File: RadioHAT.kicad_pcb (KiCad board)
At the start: 2 copper layers, 65 x 56.5 mm, 37 parts, among them J1 RPi_GPIO, J3 Conn_02x06_Odd_Even, J4 Conn_02x07_Odd_Even, U1 INA219AxD, U2 LP3855-ADJ

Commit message: [PCB] Add jumper texts
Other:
- board text added: "INA_BYPASS"
- board text added: "PWR_LDO"
- board text added: "PWR_RPI"
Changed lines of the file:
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@@
 			(at 0 1.8288 0)
 			(layer "F.SilkS")
+			(hide yes)
 			(effects
 				(font
@@
 			(at 0 -1.8 90)
 			(layer "F.SilkS")
+			(hide yes)
 			(effects
 				(font
@@
 			(layer "F.CrtYd")
 		)
-		(fp_text user "3"
-			(at 2.6 0 90)
-			(layer "F.SilkS")
-			(effects
-				(font
-					(size 1 1)
-					(thickness 0.15)
-				)
-			)
-		)
-		(fp_text user "1"
-			(at -2.6 0 90)
-			(layer "F.SilkS")
-			(effects
-				(font
-					(size 1 1)
-					(thickness 0.15)
-				)
-			)
-		)
 		(pad "1" smd rect
 			(at -1.3 0 270)
@@
 			(at 0 -1.8 90)
 			(layer "F.SilkS")
+			(hide yes)
 			(effects
 				(font
@@
 			(layer "F.CrtYd")
 		)
-		(fp_text user "3"
-			(at 2.6 0 90)
-			(layer "F.SilkS")
-			(effects
-				(font
-					(size 1 1)
-					(thickness 0.15)
-				)
-			)
-		)
-		(fp_text user "1"
-			(at -2.6 0 90)
-			(layer "F.SilkS")
-			(effects
-				(font
-					(size 1 1)
-					(thickness 0.15)
-				)
-			)
-		)
 		(pad "1" smd rect
 			(at -1.3 0 270)
@@
 			(at 0 -1.8 90)
 			(layer "F.SilkS")
+			(hide yes)
 			(effects
 				(font
@@
 			(layer "F.CrtYd")
 		)
-		(fp_text user "1"
-			(at -2.6 0 90)
-			(layer "F.SilkS")
-			(effects
-				(font
-					(size 1 1)
-					(thickness 0.15)
-				)
-			)
-		)
-		(fp_text user "3"
-			(at 2.6 0 90)
-			(layer "F.SilkS")
-			(effects
-				(font
-					(size 1 1)
-					(thickness 0.15)
-				)
-			)
-		)
 		(pad "1" smd rect
 			(at -1.3 0 270)
@@
 		)
 	)
+	(gr_text "PWR_LDO"
+		(at 149.7584 90.6272 0)
+		(layer "F.SilkS")
+		(effects
+			(font
+				(size 0.6 0.6)
+				(thickness 0.1)
+			)
+			(justify left)
+		)
+	)
+	(gr_text "INA_BYPASS"
+		(at 157.6324 90.0684 0)
+		(layer "F.SilkS")
+		(effects
+			(font
+				(size 0.6 0.6)
+				(thickness 0.1)
+			)
+			(justify bottom)
+		)
+	)
+	(gr_text "PWR_RPI"
+		(at 149.8092 92.3036 0)
+		(layer "F.SilkS")
+		(effects
+			(font
+				(size 0.6 0.6)
+				(thickness 0.1)
+			)
+			(justify left)
+		)
+	)

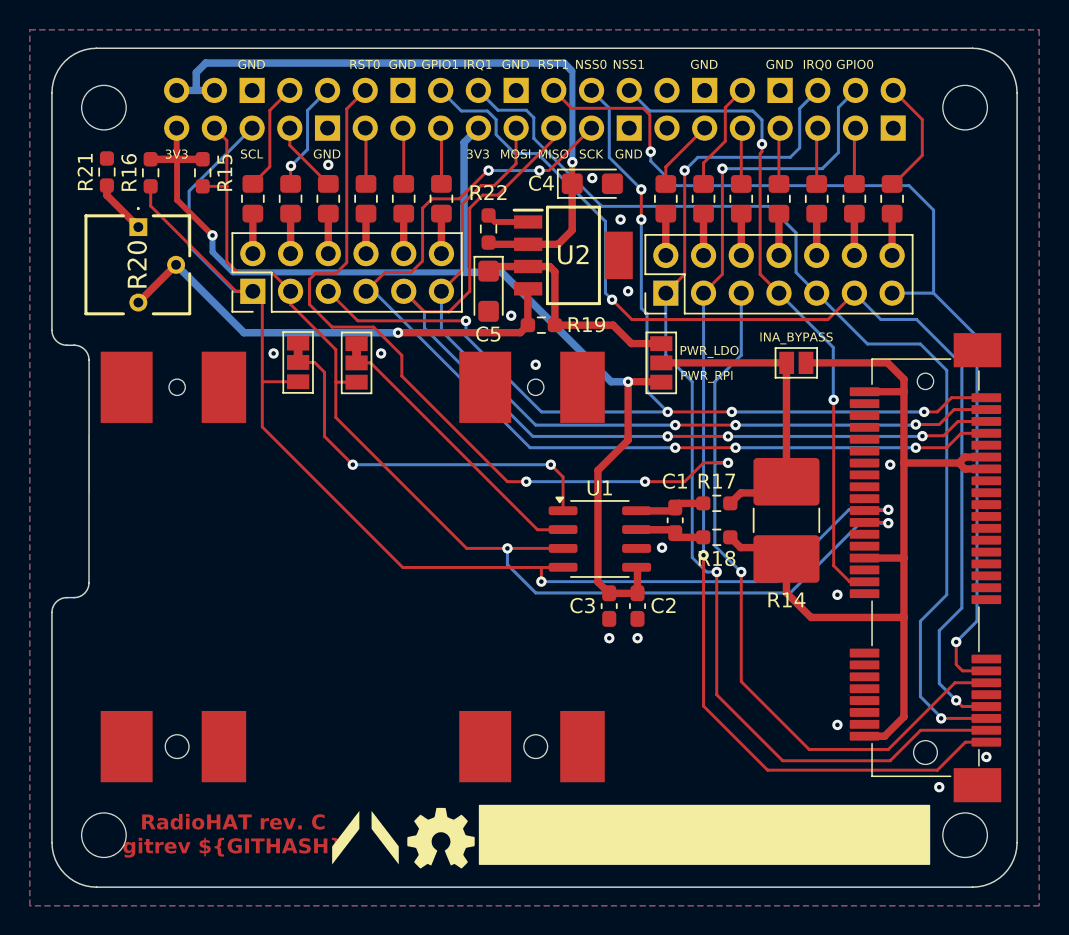
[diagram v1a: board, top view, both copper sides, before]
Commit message: Implemented @RemyChatel recommendations
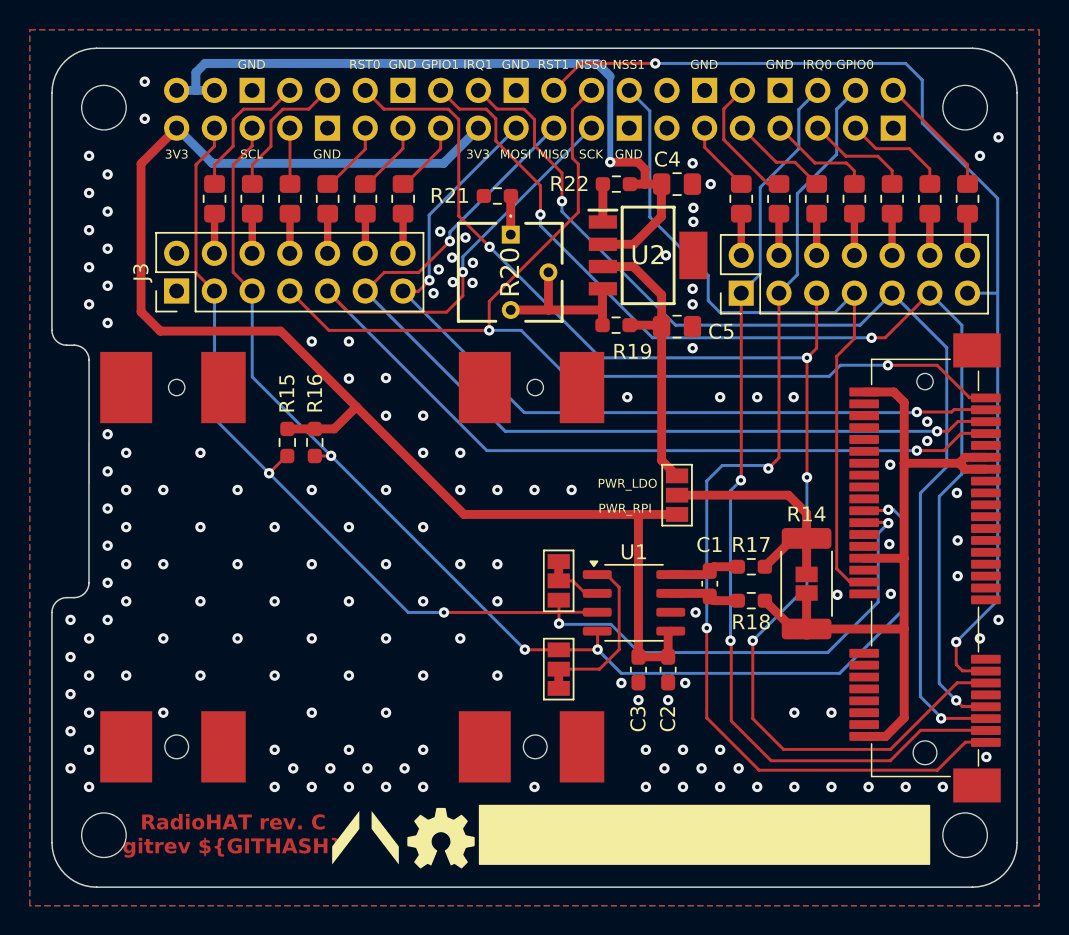
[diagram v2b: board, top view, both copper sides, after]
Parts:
- removed JP4: SolderJumper_2_Open, Jumper:SolderJumper-2_P1.3mm_Open_Pad1.0x1.5mm
- C4, C5: value 10u -> 100n; footprint Capacitor_Tantalum_SMD:CP_EIA-3216-18_Kemet-A -> Capacitor_SMD:C_0805_2012Metric_Pad1.18x1.45mm_HandSolder
- J3: value Conn_02x06_Odd_Even -> Conn_02x07_Odd_Even; footprint Connector_PinHeader_2.54mm:PinHeader_2x06_P2.54mm_Vertical -> Connector_PinHeader_2.54mm:PinHeader_2x07_P2.54mm_Vertical
- R14: footprint Resistor_SMD:R_2816_7142Metric_Pad3.20x4.45mm_HandSolder -> RadioHAT:R_2512_6332Metric_Pad1.40x3.35mm_HandSolder_Bypass
- R19: value 100R -> 10k
- R20: value 18R -> 2k; footprint RadioHAT:3362P1200LF -> RadioHAT:Potentiometer_Bourns_3362P1200LF
- R21: value 51R -> 6.8k
- moved JP2 27.1 mm to (141.6, 112.1), turned to 90 degrees
- moved R21 26.3 mm to (137.5, 80.2), turned to 180 degrees
- moved R20 25.1 mm to (138.4, 82.8)
- moved R16 21.3 mm to (125.2, 96.8)
- moved JP1 20.0 mm to (141.6, 106.1)
- moved R15 19.0 mm to (123.3, 96.8)
- moved C5 12.9 mm to (149.6, 89.0), turned to 0 degrees
- moved R22 9.13 mm to (145.5, 79.4), turned to 180 degrees
- moved JP5 8.97 mm to (149.6, 100.3)
- moved C4 5.71 mm to (149.6, 79.4)
- moved J3 5.13 mm to (115.9, 86.6)
- moved J4 5.08 mm to (153.9, 86.7)
- moved R10 5.08 mm to (161.5, 80.4)
- moved R11 5.08 mm to (164.1, 80.4)
- moved R7 5.08 mm to (153.9, 80.4)
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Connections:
- J1 pad 10: SDA_SENSE -> SCL_SENSE
- J1 pad 8: SCL_SENSE -> SDA_SENSE
- J3 pad 1: SCL -> GND
- J3 pad 11: MOSI -> MISO
- J3 pad 2: Net-(J3-Pin_2) -> GND
- J3 pad 5: NSS0 -> SCL
- J3 pad 7: SCK -> NSS0
- J3 pad 9: MISO -> SCK
- R1 pad 1: Net-(J3-Pin_2) -> Net-(J3-Pin_4)
- R1 pad 2: SCL_SENSE -> SDA_SENSE
- R2 pad 1: Net-(J3-Pin_4) -> Net-(J3-Pin_6)
- R2 pad 2: SDA_SENSE -> SCL_SENSE
- R3 pad 1: Net-(J3-Pin_6) -> Net-(J3-Pin_8)
- R4 pad 1: Net-(J3-Pin_8) -> Net-(J3-Pin_10)
- R5 pad 1: Net-(J3-Pin_10) -> Net-(J3-Pin_12)
- R6 pad 1: Net-(J3-Pin_12) -> Net-(J3-Pin_14)
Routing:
- net Net-(U2-ADJ): track 31.6 -> 11.2 mm, vias 1 -> 0
- net +3.3V: track 76.7 -> 96.1 mm, vias 2 -> 0
- net Net-(JP1-C): track 18.6 -> 2.94 mm
- net Net-(JP2-C): track 25.9 -> 10.6 mm, vias 2 -> 0
- net +3.3V_PCI: track 61.4 -> 48.0 mm
- net RST0: track 100.1 -> 89.9 mm
- net SDA: track 77.3 -> 86.1 mm, vias 2 -> 4
- net IRQ0: track 71.4 -> 64.1 mm
- net SCL: track 89.8 -> 83.2 mm, vias 2 -> 4
- net Net-(JP5-C): track 20.8 -> 14.5 mm
- net SCK: track 68.4 -> 74.3 mm, vias 5 -> 2
- net RST1: track 68.1 -> 72.9 mm
- net +5V: track 46.3 -> 50.6 mm
- net NSS1: track 44.4 -> 48.4 mm, vias 2 -> 0
- net Net-(JP5-A): track 15.8 -> 19.6 mm
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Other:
- board text removed: "INA_BYPASS"

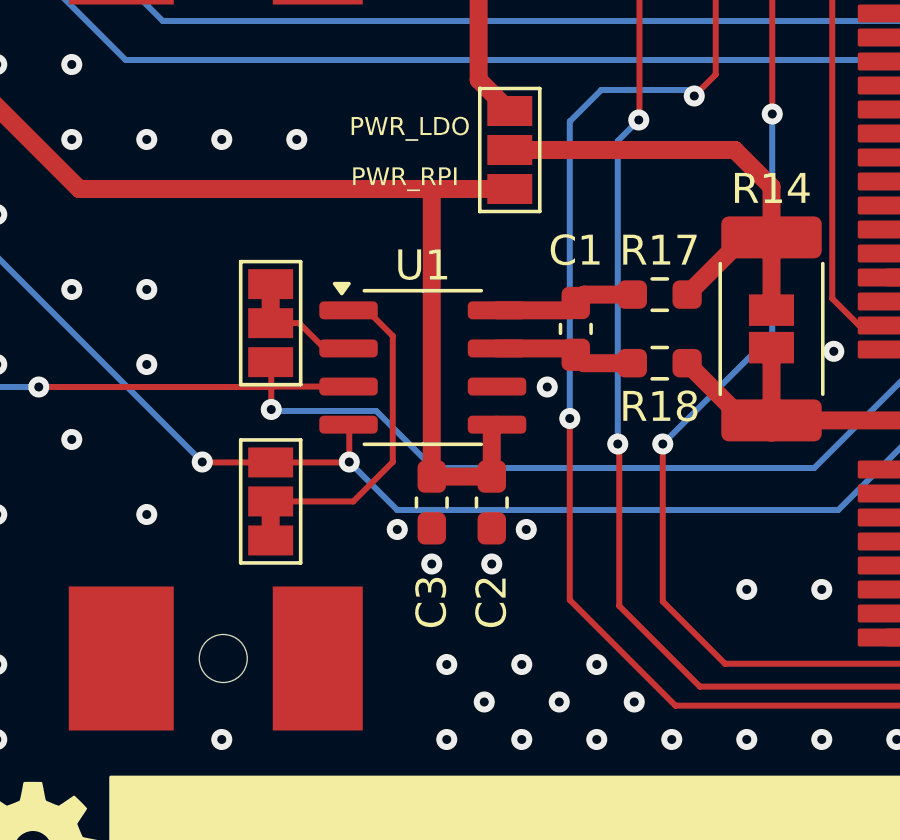
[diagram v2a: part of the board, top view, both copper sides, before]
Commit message: [PCB] Use the same package for all 10u caps
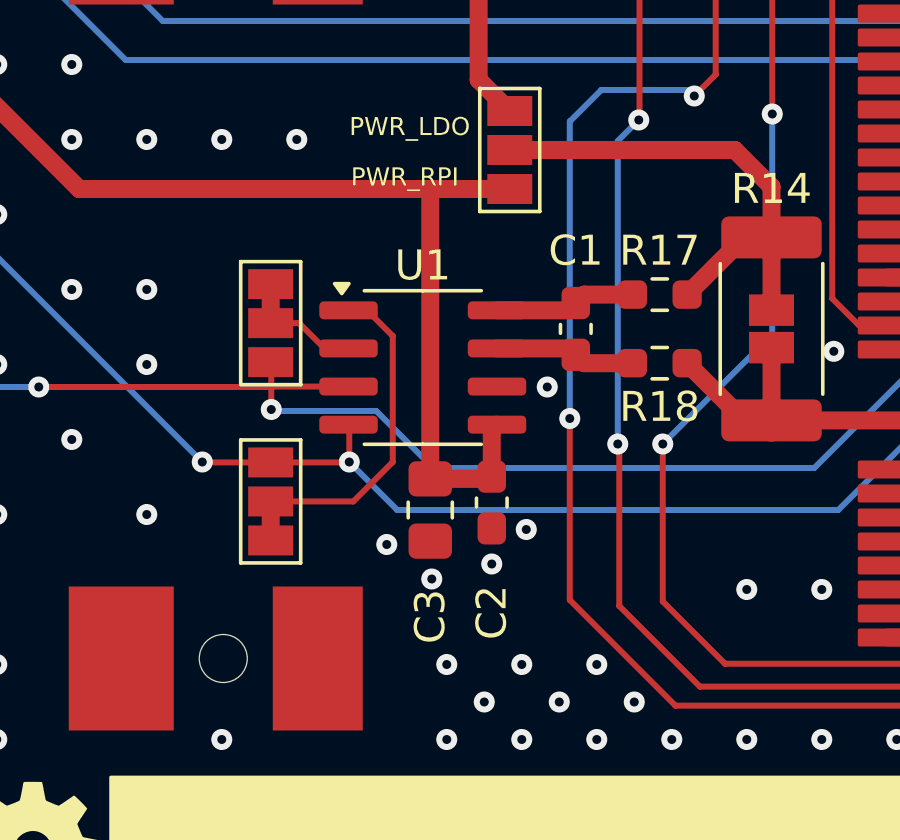
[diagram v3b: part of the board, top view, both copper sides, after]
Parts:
- C3: footprint Capacitor_SMD:C_0603_1608Metric_Pad1.08x0.95mm_HandSolder -> Capacitor_SMD:C_0805_2012Metric_Pad1.18x1.45mm_HandSolder
- C4, C5: value 100n -> 10u
- moved C3 0.25 mm to (146.9, 112.3)
